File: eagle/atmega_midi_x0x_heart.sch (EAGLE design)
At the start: 33 parts, among them IC1 TL072P, J11_VCF_CUTOFF 22-23-2021, U1 ATMEGA328P_PDIP

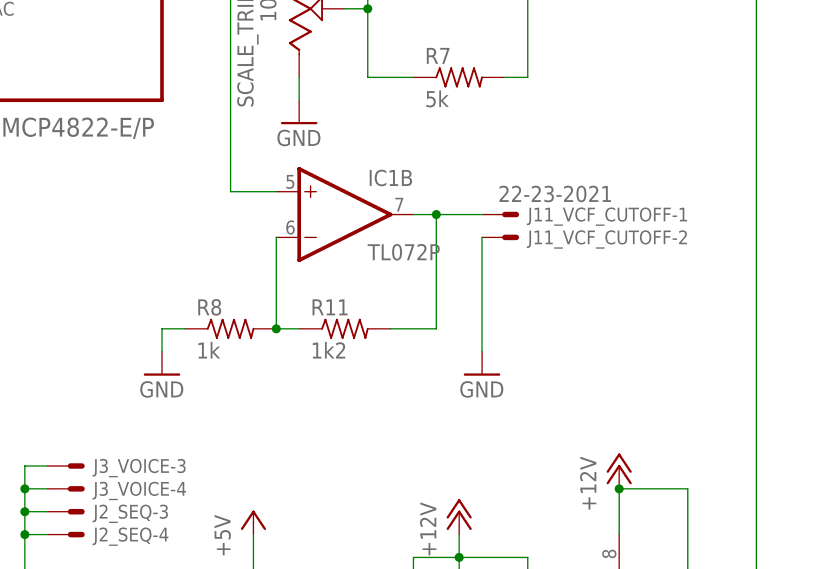
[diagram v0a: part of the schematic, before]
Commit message: added vcf output resistor
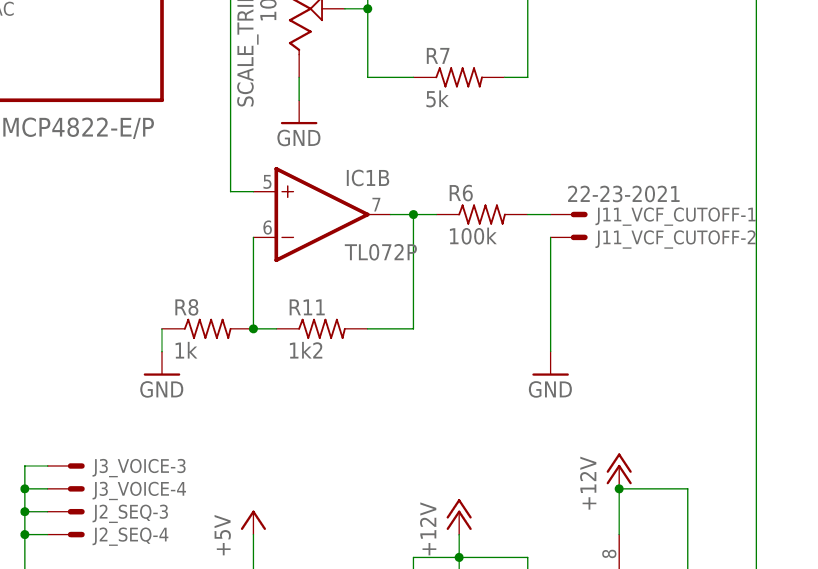
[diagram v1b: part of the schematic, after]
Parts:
- added R6: 100k, rcl:R-US_0207/10
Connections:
- new net N$29: J11_VCF_CUTOFF-1.S, R6.2
- net N$17: now also R6.1; no longer J11_VCF_CUTOFF-1.S
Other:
- moved on the sheet: IC1B, J11_VCF_CUTOFF-1, J11_VCF_CUTOFF-2, R11, R8
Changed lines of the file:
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@@
 <part name="GATE_LED" library="led" deviceset="LED" device="5MM"/>
 <part name="GND12" library="supply1" deviceset="GND" device=""/>
+<part name="R6" library="rcl" deviceset="R-US_" device="0207/10" value="100k"/>
 </parts>
 <sheets>
@@
 <instance part="SCALE_TRIM" gate="G$1" x="121.92" y="91.44" rot="MR180"/>
 <instance part="R7" gate="G$1" x="139.7" y="83.82"/>
-<instance part="R8" gate="G$1" x="114.3" y="55.88"/>
-<instance part="R11" gate="G$1" x="127" y="55.88"/>
+<instance part="R8" gate="G$1" x="111.76" y="55.88"/>
+<instance part="R11" gate="G$1" x="124.46" y="55.88"/>
 <instance part="P+6" gate="1" x="73.66" y="111.76"/>
 <instance part="U$4" gate="A" x="93.98" y="99.06"/>
@@
 <instance part="R10" gate="G$1" x="154.94" y="101.6"/>
 <instance part="IC1" gate="A" x="137.16" y="101.6"/>
-<instance part="IC1" gate="B" x="127" y="68.58"/>
+<instance part="IC1" gate="B" x="124.46" y="68.58"/>
 <instance part="IC1" gate="P" x="157.48" y="25.4"/>
-<instance part="J11_VCF_CUTOFF" gate="-1" x="144.78" y="68.58"/>
-<instance part="J11_VCF_CUTOFF" gate="-2" x="144.78" y="66.04"/>
+<instance part="J11_VCF_CUTOFF" gate="-1" x="152.4" y="68.58"/>
+<instance part="J11_VCF_CUTOFF" gate="-2" x="152.4" y="66.04"/>
 <instance part="J3_VOICE" gate="-1" x="58.42" y="25.4"/>
 <instance part="J3_VOICE" gate="-2" x="58.42" y="35.56"/>
@@
 <instance part="GND8" gate="1" x="147.32" y="10.16"/>
 <instance part="GND9" gate="1" x="157.48" y="10.16"/>
-<instance part="GND10" gate="1" x="142.24" y="50.8"/>
+<instance part="GND10" gate="1" x="149.86" y="50.8"/>
 <instance part="GND11" gate="1" x="121.92" y="78.74"/>
 <instance part="R4" gate="G$1" x="53.34" y="60.96"/>
 <instance part="GATE_LED" gate="G$1" x="63.5" y="60.96" rot="R90"/>
 <instance part="GND12" gate="1" x="73.66" y="55.88"/>
+<instance part="R6" gate="G$1" x="142.24" y="68.58"/>
 </instances>
 <busses>
@@
 <segment>
 <pinref part="R8" gate="G$1" pin="2"/>
-<wire x1="119.38" y1="66.04" x2="119.38" y2="55.88" width="0.1524" layer="91"/>
+<wire x1="116.84" y1="66.04" x2="116.84" y2="55.88" width="0.1524" layer="91"/>
 <pinref part="R11" gate="G$1" pin="1"/>
-<wire x1="121.92" y1="55.88" x2="119.38" y2="55.88" width="0.1524" layer="91"/>
-<junction x="119.38" y="55.88"/>
+<wire x1="119.38" y1="55.88" x2="116.84" y2="55.88" width="0.1524" layer="91"/>
+<junction x="116.84" y="55.88"/>
 <pinref part="IC1" gate="B" pin="-IN"/>
 </segment>
@@
 <net name="N$17" class="0">
 <segment>
-<wire x1="134.62" y1="68.58" x2="137.16" y2="68.58" width="0.1524" layer="91"/>
+<wire x1="132.08" y1="68.58" x2="134.62" y2="68.58" width="0.1524" layer="91"/>
 <pinref part="R11" gate="G$1" pin="2"/>
-<wire x1="132.08" y1="55.88" x2="137.16" y2="55.88" width="0.1524" layer="91"/>
-<wire x1="137.16" y1="55.88" x2="137.16" y2="68.58" width="0.1524" layer="91"/>
-<wire x1="142.24" y1="68.58" x2="137.16" y2="68.58" width="0.1524" layer="91"/>
-<junction x="137.16" y="68.58"/>
+<wire x1="129.54" y1="55.88" x2="134.62" y2="55.88" width="0.1524" layer="91"/>
+<wire x1="134.62" y1="55.88" x2="134.62" y2="68.58" width="0.1524" layer="91"/>
 <pinref part="IC1" gate="B" pin="OUT"/>
-<pinref part="J11_VCF_CUTOFF" gate="-1" pin="S"/>
+<pinref part="R6" gate="G$1" pin="1"/>
+<wire x1="137.16" y1="68.58" x2="134.62" y2="68.58" width="0.1524" layer="91"/>
+<junction x="134.62" y="68.58"/>
 </segment>
 </net>
@@
 <net name="N$14" class="0">
 <segment>
-<wire x1="119.38" y1="71.12" x2="114.3" y2="71.12" width="0.1524" layer="91"/>
+<wire x1="116.84" y1="71.12" x2="114.3" y2="71.12" width="0.1524" layer="91"/>
 <wire x1="114.3" y1="71.12" x2="114.3" y2="101.6" width="0.1524" layer="91"/>
 <pinref part="U$4" gate="A" pin="VOUTB"/>
@@
 <wire x1="106.68" y1="53.34" x2="106.68" y2="55.88" width="0.1524" layer="91"/>
 <pinref part="R8" gate="G$1" pin="1"/>
-<wire x1="106.68" y1="55.88" x2="109.22" y2="55.88" width="0.1524" layer="91"/>
 <pinref part="GND6" gate="1" pin="GND"/>
 </segment>
@@
 <segment>
 <pinref part="J11_VCF_CUTOFF" gate="-2" pin="S"/>
-<wire x1="142.24" y1="53.34" x2="142.24" y2="66.04" width="0.1524" layer="91"/>
+<wire x1="149.86" y1="53.34" x2="149.86" y2="66.04" width="0.1524" layer="91"/>
 <pinref part="GND10" gate="1" pin="GND"/>
 </segment>
@@
 </segment>
 </net>
+<net name="N$29" class="0">
+<segment>
+<pinref part="J11_VCF_CUTOFF" gate="-1" pin="S"/>
+<pinref part="R6" gate="G$1" pin="2"/>
+<wire x1="147.32" y1="68.58" x2="149.86" y2="68.58" width="0.1524" layer="91"/>
+</segment>
+</net>

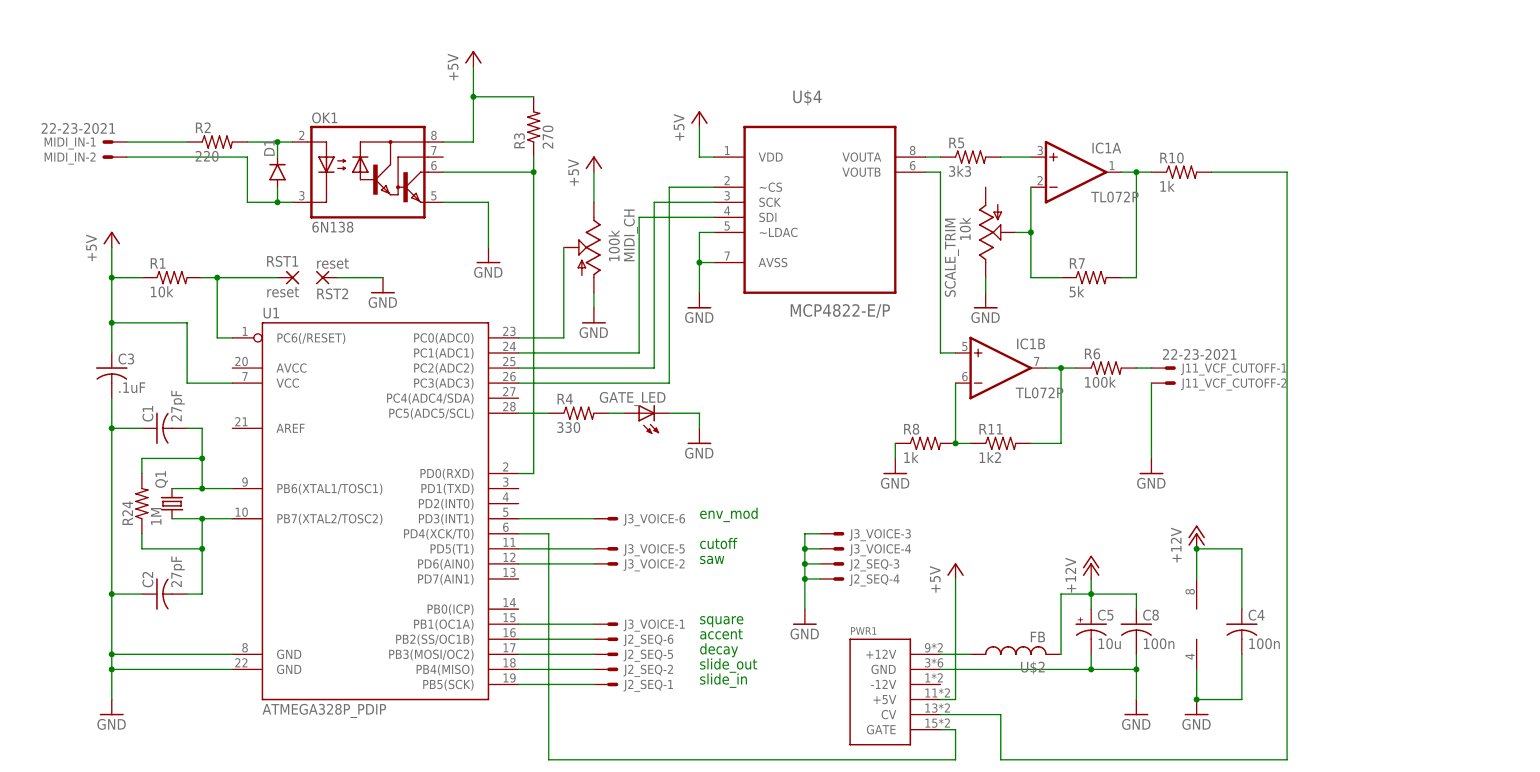
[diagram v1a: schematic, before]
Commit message: changed to TI precision opamp
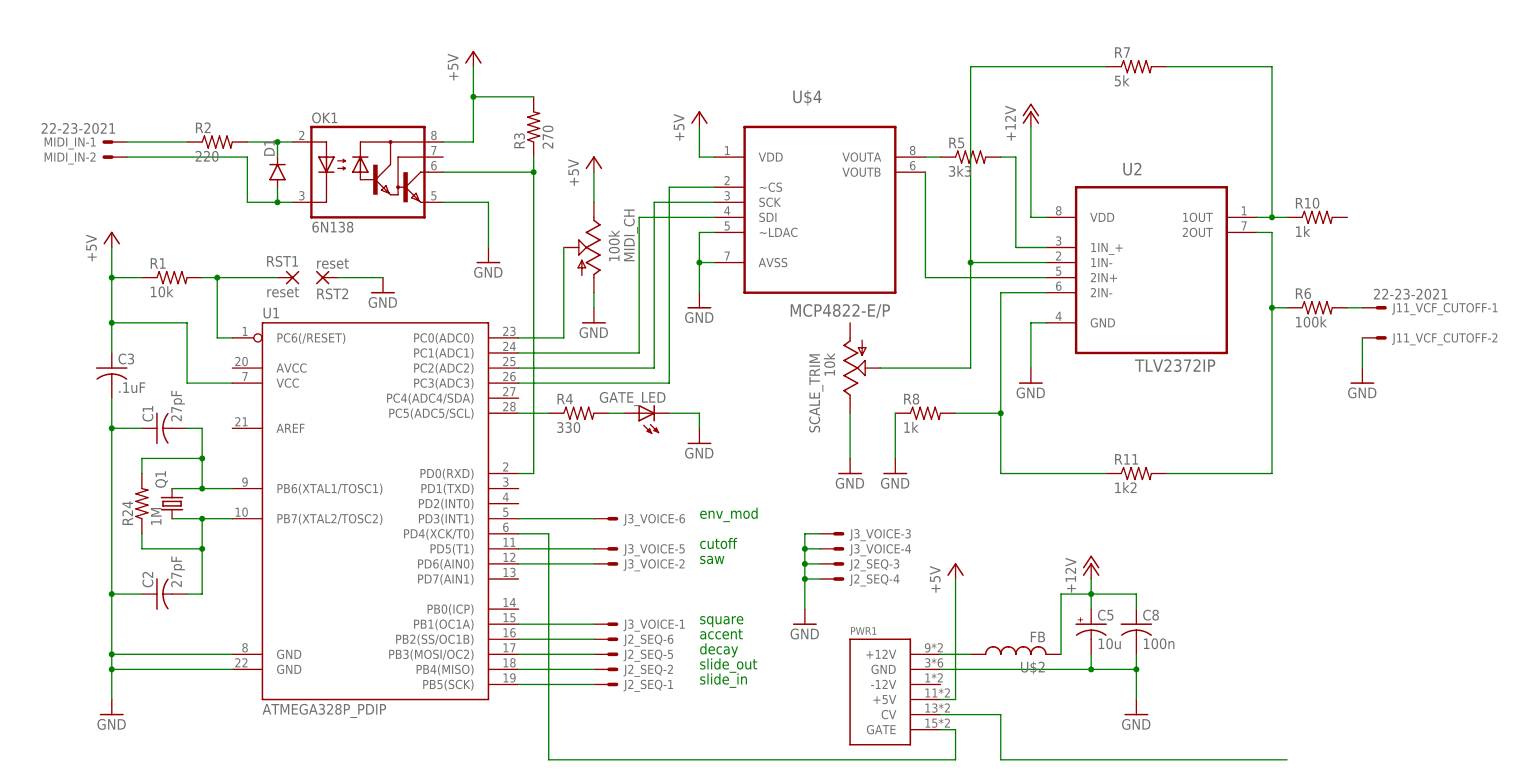
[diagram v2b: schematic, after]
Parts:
- removed C4: 100n, rcl:C-US050-024X044
- removed IC1: TL072P, linear:TL072P
- added U2: TLV2372IP, Texas Instruments_By_element14_Batch_1:TLV2372IP
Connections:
- net +12V: now also U2.VDD; no longer C4.1, IC1P.V+
- net GND: now also U2.GND; no longer C4.2, IC1P.V-
- net N$12: now also U2.1IN-; no longer IC1A.-IN
- net N$13: now also U2.2IN-; no longer IC1B.-IN
- net N$14: now also U2.2IN+; no longer IC1B.+IN
- net N$15: no longer R10.2
- net N$17: now also U2.2OUT; no longer IC1B.OUT
- net N$27: now also U2.1OUT; no longer IC1A.OUT
- net N$6: now also U2.1IN_+; no longer IC1A.+IN
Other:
- moved on the sheet: J11_VCF_CUTOFF-1, J11_VCF_CUTOFF-2, R10, R11, R6, R7, R8, SCALE_TRIM

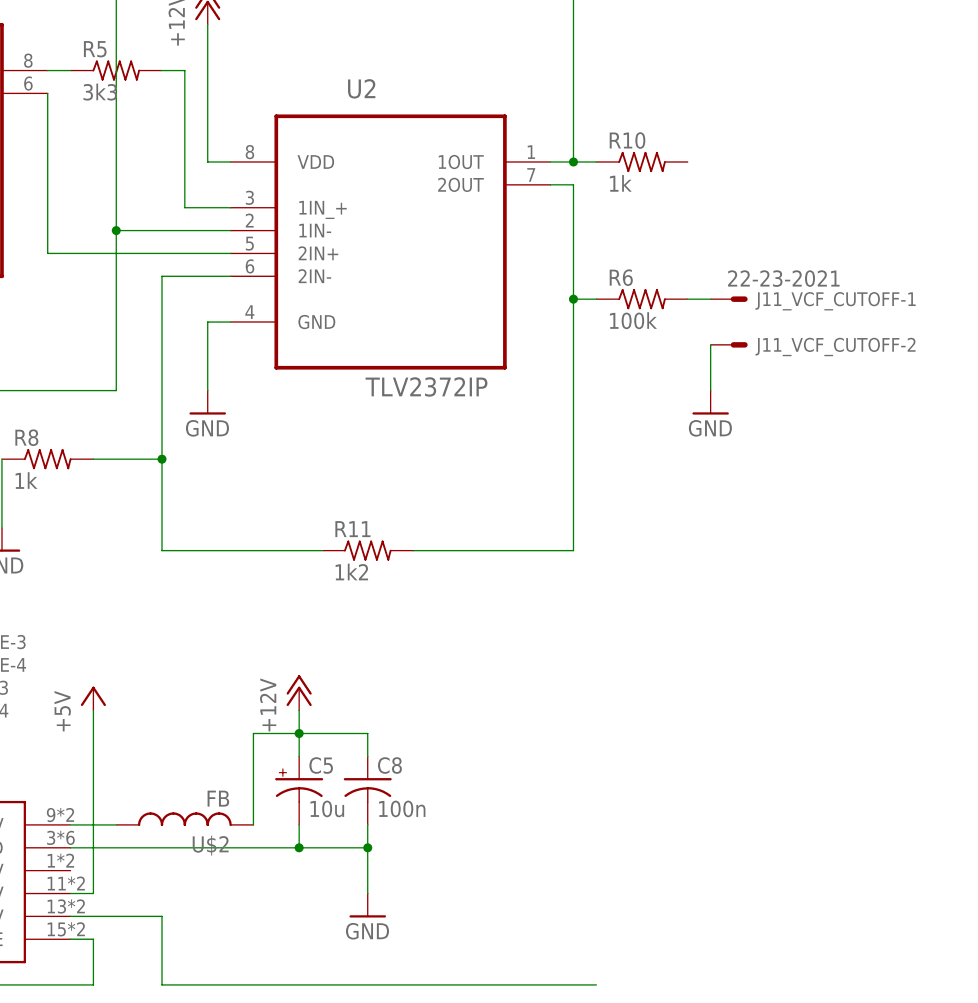
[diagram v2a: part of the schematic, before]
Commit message: tweaked cutout for better holes
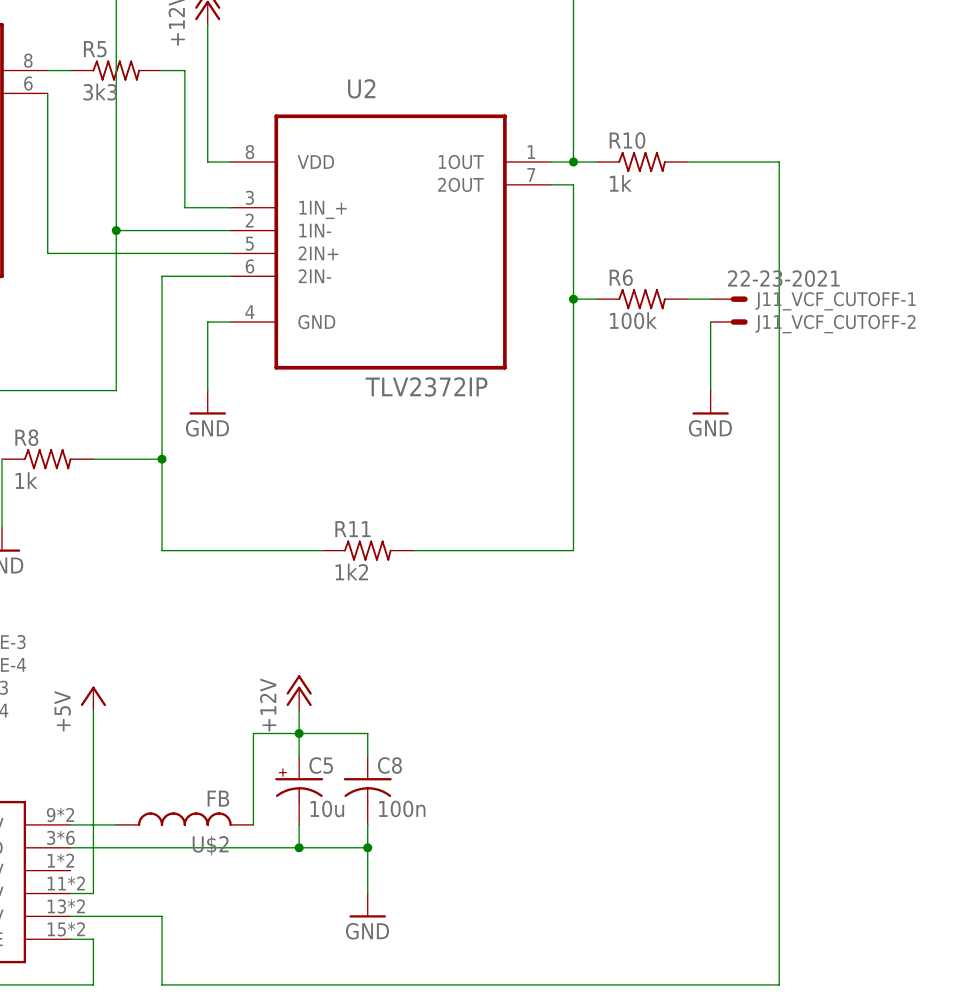
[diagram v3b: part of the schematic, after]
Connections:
- net N$15: now also R10.2
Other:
- moved on the sheet: J11_VCF_CUTOFF-2
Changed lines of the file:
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@@
 <instance part="R10" gate="G$1" x="177.8" y="93.98"/>
 <instance part="J11_VCF_CUTOFF" gate="-1" x="187.96" y="78.74"/>
-<instance part="J11_VCF_CUTOFF" gate="-2" x="187.96" y="73.66"/>
+<instance part="J11_VCF_CUTOFF" gate="-2" x="187.96" y="76.2"/>
 <instance part="J3_VOICE" gate="-1" x="58.42" y="25.4"/>
 <instance part="J3_VOICE" gate="-2" x="58.42" y="35.56"/>
@@
 <net name="N$15" class="0">
 <segment>
-<wire x1="124.46" y1="2.54" x2="172.72" y2="2.54" width="0.1524" layer="91"/>
+<wire x1="124.46" y1="2.54" x2="193.04" y2="2.54" width="0.1524" layer="91"/>
 <wire x1="124.46" y1="10.16" x2="124.46" y2="2.54" width="0.1524" layer="91"/>
 <pinref part="PWR1" gate="G$1" pin="CV"/>
 <wire x1="114.3" y1="10.16" x2="124.46" y2="10.16" width="0.1524" layer="91"/>
+<wire x1="193.04" y1="2.54" x2="193.04" y2="93.98" width="0.1524" layer="91"/>
+<pinref part="R10" gate="G$1" pin="2"/>
+<wire x1="193.04" y1="93.98" x2="182.88" y2="93.98" width="0.1524" layer="91"/>
 </segment>
 </net>
@@
 <segment>
 <pinref part="J11_VCF_CUTOFF" gate="-2" pin="S"/>
-<wire x1="185.42" y1="68.58" x2="185.42" y2="73.66" width="0.1524" layer="91"/>
+<wire x1="185.42" y1="68.58" x2="185.42" y2="76.2" width="0.1524" layer="91"/>
 <pinref part="GND10" gate="1" pin="GND"/>
 </segment>

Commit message: digital pot and midi out
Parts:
- added MIDI_OUT_THRU, RES1, RES2, RES_POT: (no value), con-lstb:MA03-1
- added R9: 220, rcl:R-US_0207/10
- added U$1: MCP42050-E/P, MCP42050-E_P:MCP42050-E/P
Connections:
- new net N$31: RES1.2, U$1.PW0
- new net N$32: RES1.1, U$1.PA0
- new net N$33: RES1.3, U$1.PB0
- new net N$34: RES2.2, U$1.PW1
- new net N$35: RES2.1, U$1.PA1
- new net N$36: RES2.3, U$1.PB1
- new net N$37: U$1.SI, U1.PB0(ICP)
- new net N$38: RES_POT.2, U1.PC4(ADC4/SDA)
- new net N$39: MIDI_OUT_THRU.1, R9.2
- new net N$40: U$1.~CS, U1.PD2(INT0)
- new net N$41: U$1.SCK, U1.PD7(AIN1)
- new net N$42: MIDI_OUT_THRU.2, U1.PD1(TXD)
- net +5V: now also R9.1, RES_POT.1, U$1.VDD, U$1.~RS, U$1.~SHDN, U1.AREF
- net GND: now also MIDI_OUT_THRU.3, RES_POT.3, U$1.VSS
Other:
- moved on the sheet: C5, C8, J2_SEQ-1, J2_SEQ-2, J2_SEQ-3, J2_SEQ-4, J2_SEQ-5, J2_SEQ-6, J3_VOICE-1, J3_VOICE-2, J3_VOICE-3, J3_VOICE-4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
